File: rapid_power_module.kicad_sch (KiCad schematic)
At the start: 206 parts, among them J1 Conn_02x04_Top_Bottom, J10 JST-GH 4Pin, J11 SWD Header, J12 SWD Header, J16 USB_C_Receptacle_USB2.0, J17 TC2050, J2 Conn_02x03_Odd_Even, J3 Conn_02x04_Top_Bottom, J4 Conn_02x03_Odd_Even, J5 Molex MicroFit 2x2, J6 Molex MicroFit 2x2, J7 Molex MicroFit 2x2, J8 Molex MicroFit 2x2, Q1 AOSP21321, Q12 AOSP21321, Q2 AOSP21321, Q3 AOSP21321, Q4 HiDRV1, Q5 LoDRV1, Q6 HiDRV2, Q7 LoDRV2, SW1 KMR721NGLFS, SW2 KMR721NGLFS, U1 BQ25756RRVR, U10 L7805, U11 MCP2562-E-SN, U12 STM32F105RCTx, U13 AZ1117I-3.3, U14 TPD4E1U06, U15 TPD4E1U06, U2 CYPD3177-24LQ, U3 BQ76952PFBR, Y3 8MHz 12pF

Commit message: more routing work
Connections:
- net CHRG_IND_LED_1: now also U12.54 (PD2); no longer U12.33 (PB12)
- net CHRG_IND_LED_2: now also U12.55 (PB3); no longer U12.34 (PB13)
- net CHRG_IND_LED_3: now also U12.56 (PB4); no longer U12.35 (PB14)
- net CHRG_IND_LED_4: now also U12.57 (PB5); no longer U12.36 (PB15)
- net D0+: now also U14.5 (IO4); no longer U14.4 (IO3)
- net D0-: now also U14.4 (IO3); no longer U14.5 (IO4)
- net INT: now also U12.51 (PC10); no longer U12.25 (PC5)
- net PG: now also U12.36 (PB15); no longer U12.39 (PC8)
- net STAT_LED0: now also U12.33 (PB12); no longer U12.2 (PC13)
- net STAT_LED1: now also U12.34 (PB13); no longer U12.3 (PC14)
- net STAT_LED2: now also U12.35 (PB14); no longer U12.4 (PC15)
- net USB_PD_INTERRUPT: now also U12.29 (PB10); no longer U12.21 (PA5)
- no-connect marks 35 -> 33
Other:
- note added: "Mv usb int from 21 to 29"
- note added: "int from 25 to 51 PG from 39 to 36"

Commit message: more routing
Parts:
- D4: footprint Package_TO_SOT_THT:TO-220-3_Vertical -> Diode_SMD:D_SOD-323; LCSC C5358933 -> C191023
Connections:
- net BREG: now also U12.4 (PC15)
- net REGIN: now also U12.3 (PC14)
- net RST_SHUT: now also U12.2 (PC13); no longer U12.16 (PA2)
- no-connect marks 33 -> 31
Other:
- note added: "int from 25 to 51 PG from 39 to 36 REGIN und BREG verbunden mit STM32"
- note added: "mv 16 -> 2"
- note removed: "int from 25 to 51 PG from 39 to 36"
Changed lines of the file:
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@@
 		)
 	)
-	(text "int from 25 to 51\nPG from 39 to 36"
+	(text "int from 25 to 51\nPG from 39 to 36\nREGIN und BREG verbunden mit STM32"
 		(exclude_from_sim no)
-		(at 113.792 326.644 0)
+		(at 108.458 330.708 0)
 		(effects
 			(font
@@
 		)
 	)
+	(text "mv 16 -> 2"
+		(exclude_from_sim no)
+		(at 171.45 267.97 0)
+		(effects
+			(font
+				(size 1.27 1.27)
+			)
+		)
+	)
 	(text "@todo: take a closer look"
 		(exclude_from_sim no)
@@
 	)
 	(no_connect
-		(at 127 323.85)
-	)
-	(no_connect
 		(at 488.95 130.81)
 	)
@@
 	)
 	(no_connect
+		(at 162.56 270.51)
+	)
+	(no_connect
 		(at 488.95 123.19)
 	)
@@
 	)
 	(no_connect
-		(at 127 318.77)
-	)
-	(no_connect
-		(at 127 321.31)
-	)
-	(no_connect
 		(at 488.95 110.49)
 	)
@@
 	(wire
 		(pts
-			(xy 165.1 270.51) (xy 162.56 270.51)
-		)
-		(stroke
-			(width 0)
-			(type default)
-		)
-	)
-	(wire
-		(pts
 			(xy 205.74 167.64) (xy 203.2 167.64)
 		)
@@
 	(global_label "RST_SHUT"
 		(shape input)
-		(at 165.1 270.51 0)
+		(at 127 318.77 180)
 		(fields_autoplaced yes)
 		(effects
@@
 				(size 1.27 1.27)
 			)
-			(justify left)
+			(justify right)
 		)
 		(property "Intersheetrefs" "${INTERSHEET_REFS}"
-			(at 177.338 270.51 0)
+			(at 114.762 318.77 0)
 			(effects
 				(font
 					(size 1.27 1.27)
 				)
-				(justify left)
+				(justify right)
 				(hide yes)
 			)
@@
 		)
 	)
+	(global_label "REGIN"
+		(shape input)
+		(at 127 321.31 180)
+		(fields_autoplaced yes)
+		(effects
+			(font
+				(size 1.27 1.27)
+			)
+			(justify right)
+		)
+		(property "Intersheetrefs" "${INTERSHEET_REFS}"
+			(at 118.3905 321.31 0)
+			(effects
+				(font
+					(size 1.27 1.27)
+				)
+				(justify right)
+				(hide yes)
+			)
+		)
+	)
 	(global_label "SWCLK"
 		(shape input)
@@
 		)
 	)
+	(global_label "BREG"
+		(shape input)
+		(at 127 323.85 180)
+		(fields_autoplaced yes)
+		(effects
+			(font
+				(size 1.27 1.27)
+			)
+			(justify right)
+		)
+		(property "Intersheetrefs" "${INTERSHEET_REFS}"
+			(at 119.0558 323.85 0)
+			(effects
+				(font
+					(size 1.27 1.27)
+				)
+				(justify right)
+				(hide yes)
+			)
+		)
+	)
 	(global_label "SWDIO"
 		(shape input)
@@
 			)
 		)
-		(property "Footprint" "Package_TO_SOT_THT:TO-220-3_Vertical"
+		(property "Footprint" "Diode_SMD:D_SOD-323"
 			(at 533.4 326.39 0)
 			(effects
@@
 			)
 		)
-		(property "LCSC" "C5358933"
+		(property "LCSC" "C191023"
 			(at 533.4 326.39 0)
 			(effects

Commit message: Fixed Balancer Pins so that LDO is not used and LDO input is grounded
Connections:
- net PGND: now also U3.36 (REGIN), U3.37 (BREG)
- net BREG: no longer names the net of U12.4 (PC15)
- net BREG: no longer U3.37 (BREG)
- net REGIN: no longer names the net of U12.3 (PC14)
- net REGIN: no longer U3.36 (REGIN)
- no-connect marks 31 -> 33
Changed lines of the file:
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@@
 	)
 	(junction
+		(at 490.22 115.57)
+		(diameter 0)
+		(color 0 0 0 0)
+	)
+	(junction
 		(at 233.68 123.19)
 		(diameter 0)
@@
 	)
 	(no_connect
+		(at 127 321.31)
+	)
+	(no_connect
 		(at 488.95 107.95)
 	)
 	(no_connect
+		(at 127 323.85)
+	)
+	(no_connect
 		(at 328.93 368.3)
 	)
@@
 	(wire
 		(pts
+			(xy 490.22 118.11) (xy 490.22 115.57)
+		)
+		(stroke
+			(width 0)
+			(type default)
+		)
+	)
+	(wire
+		(pts
 			(xy 30.48 349.25) (xy 30.48 356.87)
 		)
@@
 	(wire
 		(pts
+			(xy 488.95 118.11) (xy 490.22 118.11)
+		)
+		(stroke
+			(width 0)
+			(type default)
+		)
+	)
+	(wire
+		(pts
 			(xy 62.23 68.58) (xy 62.23 71.12)
 		)
@@
 	(wire
 		(pts
+			(xy 490.22 115.57) (xy 492.76 115.57)
+		)
+		(stroke
+			(width 0)
+			(type default)
+		)
+	)
+	(wire
+		(pts
 			(xy 421.64 378.46) (xy 421.64 379.73)
 		)
@@
 	(wire
 		(pts
+			(xy 490.22 115.57) (xy 488.95 115.57)
+		)
+		(stroke
+			(width 0)
+			(type default)
+		)
+	)
+	(wire
+		(pts
 			(xy 499.11 325.12) (xy 502.92 325.12)
 		)
@@
 	(wire
 		(pts
-			(xy 488.95 115.57) (xy 490.22 115.57)
-		)
-		(stroke
-			(width 0)
-			(type default)
-		)
-	)
-	(wire
-		(pts
 			(xy 353.06 328.93) (xy 353.06 365.76)
 		)
@@
 	(wire
 		(pts
-			(xy 488.95 118.11) (xy 490.22 118.11)
-		)
-		(stroke
-			(width 0)
-			(type default)
-		)
-	)
-	(wire
-		(pts
 			(xy 426.72 379.73) (xy 426.72 381)
 		)
@@
 		)
 	)
-	(global_label "REGIN"
-		(shape input)
-		(at 490.22 118.11 0)
-		(fields_autoplaced yes)
-		(effects
-			(font
-				(size 1.27 1.27)
-			)
-			(justify left)
-		)
-		(property "Intersheetrefs" "${INTERSHEET_REFS}"
-			(at 498.8295 118.11 0)
-			(effects
-				(font
-					(size 1.27 1.27)
-				)
-				(justify left)
-				(hide yes)
-			)
-		)
-	)
 	(global_label "USB_D-"
 		(shape input)
@@
 		)
 	)
-	(global_label "REGIN"
-		(shape input)
-		(at 127 321.31 180)
-		(fields_autoplaced yes)
-		(effects
-			(font
-				(size 1.27 1.27)
-			)
-			(justify right)
-		)
-		(property "Intersheetrefs" "${INTERSHEET_REFS}"
-			(at 118.3905 321.31 0)
-			(effects
-				(font
-					(size 1.27 1.27)
-				)
-				(justify right)
-				(hide yes)
-			)
-		)
-	)
 	(global_label "SWCLK"
 		(shape input)
@@
 		)
 	)
-	(global_label "BREG"
-		(shape input)
-		(at 490.22 115.57 0)
-		(fields_autoplaced yes)
-		(effects
-			(font
-				(size 1.27 1.27)
-			)
-			(justify left)
-		)
-		(property "Intersheetrefs" "${INTERSHEET_REFS}"
-			(at 498.1642 115.57 0)
-			(effects
-				(font
-					(size 1.27 1.27)
-				)
-				(justify left)
-				(hide yes)
-			)
-		)
-	)
 	(global_label "CE"
 		(shape input)
@@
 		)
 	)
-	(global_label "BREG"
-		(shape input)
-		(at 127 323.85 180)
-		(fields_autoplaced yes)
-		(effects
-			(font
-				(size 1.27 1.27)
-			)
-			(justify right)
-		)
-		(property "Intersheetrefs" "${INTERSHEET_REFS}"
-			(at 119.0558 323.85 0)
-			(effects
-				(font
-					(size 1.27 1.27)
-				)
-				(justify right)
-				(hide yes)
-			)
-		)
-	)
 	(global_label "SWDIO"
 		(shape input)
@@
 	)
 	(symbol
+		(lib_id "power:VSS")
+		(at 422.91 132.08 180)
+		(unit 1)
+		(exclude_from_sim no)
+		(in_bom yes)
+		(on_board yes)
+		(dnp no)
+		(property "Reference" "#PWR053"
+			(at 422.91 128.27 0)
+			(effects
+				(font
+					(size 1.27 1.27)
+				)
+				(hide yes)
+			)
+		)
+		(property "Value" "VSS"
+			(at 423.164 135.89 0)
+			(effects
+				(font
+					(size 1.27 1.27)
+				)
+			)
+		)
+		(property "Footprint" ""
+			(at 422.91 132.08 0)
+			(effects
+				(font
+					(size 1.27 1.27)
+				)
+				(hide yes)
+			)
+		)
+		(property "Datasheet" ""
+			(at 422.91 132.08 0)
+			(effects
+				(font
+					(size 1.27 1.27)
+				)
+				(hide yes)
+			)
+		)
+		(property "Description" "Power symbol creates a global label with name \"VSS\""
+			(at 422.91 132.08 0)
+			(effects
+				(font
+					(size 1.27 1.27)
+				)
+				(hide yes)
+			)
+		)
+		(pin "1"
+		)
+		(instances
+			(project "rapid_power_module"
+				(path "/afc8cbd3-9ea8-40a2-afae-ed6bd0fe7e6e"
+					(reference "#PWR053")
+					(unit 1)
+				)
+			)
+		)
+	)
+	(symbol
 		(lib_id "Device:C")
 		(at 158.75 250.19 0)
@@
 	)
 	(symbol
+		(lib_id "power:VSS")
+		(at 492.76 115.57 180)
+		(unit 1)
+		(exclude_from_sim no)
+		(in_bom yes)
+		(on_board yes)
+		(dnp no)
+		(property "Reference" "#PWR052"
+			(at 492.76 111.76 0)
+			(effects
+				(font
+					(size 1.27 1.27)
+				)
+				(hide yes)
+			)
+		)
+		(property "Value" "VSS"
+			(at 493.014 119.38 0)
+			(effects
+				(font
+					(size 1.27 1.27)
+				)
+			)
+		)
+		(property "Footprint" ""
+			(at 492.76 115.57 0)
+			(effects
+				(font
+					(size 1.27 1.27)
+				)
+				(hide yes)
+			)
+		)
+		(property "Datasheet" ""
+			(at 492.76 115.57 0)
+			(effects
+				(font
+					(size 1.27 1.27)
+				)
+				(hide yes)
+			)
+		)
+		(property "Description" "Power symbol creates a global label with name \"VSS\""
+			(at 492.76 115.57 0)
+			(effects
+				(font
+					(size 1.27 1.27)
+				)
+				(hide yes)
+			)
+		)
+		(pin "1"
+		)
+		(instances
+			(project "rapid_power_module"
+				(path "/afc8cbd3-9ea8-40a2-afae-ed6bd0fe7e6e"
+					(reference "#PWR052")
+					(unit 1)
+				)
+			)
+		)
+	)
+	(symbol
 		(lib_id "power:GND")
 		(at 349.25 336.55 0)
@@
 					(unit 1)
 				)
-			)
-		)
-	)
-	(symbol
-		(lib_id "power:GND1")
-		(at 422.91 132.08 0)
-		(mirror y)
-		(unit 1)
-		(exclude_from_sim no)
-		(in_bom yes)
-		(on_board yes)
-		(dnp no)
-		(property "Reference" "#PWR029"
-			(at 422.91 138.43 0)
-			(effects
-				(font
-					(size 1.27 1.27)
-				)
-				(hide yes)
-			)
-		)
-		(property "Value" "PGND"
-			(at 422.91 137.16 0)
-			(effects
-				(font
-					(size 1.27 1.27)
-				)
-			)
-		)
-		(property "Footprint" ""
-			(at 422.91 132.08 0)
-			(effects
-				(font
-					(size 1.27 1.27)
-				)
-				(hide yes)
-			)
-		)
-		(property "Datasheet" ""
-			(at 422.91 132.08 0)
-			(effects
-				(font
-					(size 1.27 1.27)
-				)
-				(hide yes)
-			)
-		)
-		(property "Description" "Power symbol creates a global label with name \"GND1\" , ground"
-			(at 422.91 132.08 0)
-			(effects
-				(font
-					(size 1.27 1.27)
-				)
-				(hide yes)
-			)
-		)
-		(pin "1"
-		)
-		(instances
-			(project "rapid_power_module"
-				(path "/afc8cbd3-9ea8-40a2-afae-ed6bd0fe7e6e"
-					(reference "#PWR029")
-					(unit 1)
-				)

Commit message: Annotated change
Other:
- note added: "Page 75, Pin 36 and 37 <-> VSS"
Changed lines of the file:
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@@
+		)
+	)
+	(text "Page 75, Pin 36 and 37 <-> VSS"
+		(exclude_from_sim no)
+		(at 512.064 115.062 0)
+		(effects
+			(font
+				(size 1.27 1.27)
+			)
 		)
 	)

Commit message: more routing
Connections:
- net +3.3V: no longer J17.7 (Pin_7), J17.8 (Pin_8), R14.1, R15.1, R16.1, R17.1, R26.1, R39.1, R40.1, R42.1, R64.1, R69.1, R70.1, R72.1, R89.1, R90.1
- net +3V3: now also J17.7 (Pin_7), J17.8 (Pin_8), R14.1, R15.1, R16.1, R17.1, R26.1, R39.1, R40.1, R42.1, R64.1, R69.1, R70.1, R72.1, R89.1, R90.1
- net GND: now also C11.2, C12.2, C13.2, C19.1, C20.2, C21.1, C24.1, C58.1, C59.1, C60.2, C61.1, C67.2, C68.2, C69.2, C70.2, C71.2, C72.2, C73.2, C74.2, C75.2, C76.2, C77.2, C78.2, C79.1, C80.1, D20.1 (K), D21.1 (K), D24.2 (A), H1.1, H2.1, H3.1, H4.1, J1.1 (Pin_1), J1.2 (Pin_2), J11.4 (Pin_4), J12.4 (Pin_4), J16.A1 (GND), J16.A12 (GND), J16.B1 (GND), J16.B12 (GND), J16.S1 (SHIELD), J17.3 (Pin_3), J17.4 (Pin_4), J3.1 (Pin_1), J3.2 (Pin_2), R13.2, R19.2, R23.2, R24.2, R25.2, R27.2, R31.2, R43.2, R7.2, R76.1, R83.2, R91.1, R94.2, R95.2, R96.2, R97.2, R98.2, SW2.1 (A), U1.22 (PGND), U10.2 (GND), U11.2 (VSS), U11.8 (STBY), U12.12 (VSSA), U12.18 (VSS), U12.31 (VSS), U12.47 (VSS), U12.63 (VSS), U13.1 (GND), U14.3 (GND), U15.3 (GND), U2.19 (GND), U2.22 (GND), U2.25 (GND), U2.6 (ISNK_FINE), U3.17 (VSS), U3.18 (SRP), U3.20 (SRN), U3.36 (REGIN), U3.37 (BREG), U3.41 (LD), Y3.2, Y3.4
- net J1-SWDIO: now also U15.1 (IO1); no longer U15.2 (IO2)
- net J1-SWO: now also U15.2 (IO2); no longer U15.1 (IO1)
- net PGND: no longer C11.2, C12.2, C13.2, C19.1, C20.2, C21.1, C24.1, C58.1, C59.1, C60.2, C61.1, C67.2, C68.2, C69.2, C70.2, C71.2, C72.2, C73.2, C74.2, C75.2, C76.2, C77.2, C78.2, C79.1, C80.1, D20.1 (K), D21.1 (K), D24.2 (A), H1.1, H2.1, H3.1, H4.1, J1.1 (Pin_1), J1.2 (Pin_2), J11.4 (Pin_4), J12.4 (Pin_4), J16.A1 (GND), J16.A12 (GND), J16.B1 (GND), J16.B12 (GND), J16.S1 (SHIELD), J17.3 (Pin_3), J17.4 (Pin_4), J3.1 (Pin_1), J3.2 (Pin_2), R13.2, R19.2, R23.2, R24.2, R25.2, R27.2, R31.2, R43.2, R7.2, R76.1, R83.2, R91.1, R94.2, R95.2, R96.2, R97.2, R98.2, SW2.1 (A), U1.22 (PGND), U10.2 (GND), U11.2 (VSS), U11.8 (STBY), U12.12 (VSSA), U12.18 (VSS), U12.31 (VSS), U12.47 (VSS), U12.63 (VSS), U13.1 (GND), U14.3 (GND), U15.3 (GND), U2.19 (GND), U2.22 (GND), U2.25 (GND), U2.6 (ISNK_FINE), U3.17 (VSS), U3.18 (SRP), U3.20 (SRN), U3.36 (REGIN), U3.37 (BREG), U3.41 (LD), Y3.2, Y3.4
- net STAT1: now also U12.38 (PC7); no longer U12.37 (PC6)
- net STAT2: now also U12.37 (PC6); no longer U12.38 (PC7)
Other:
- note added: "@TODO sinnvoll?"

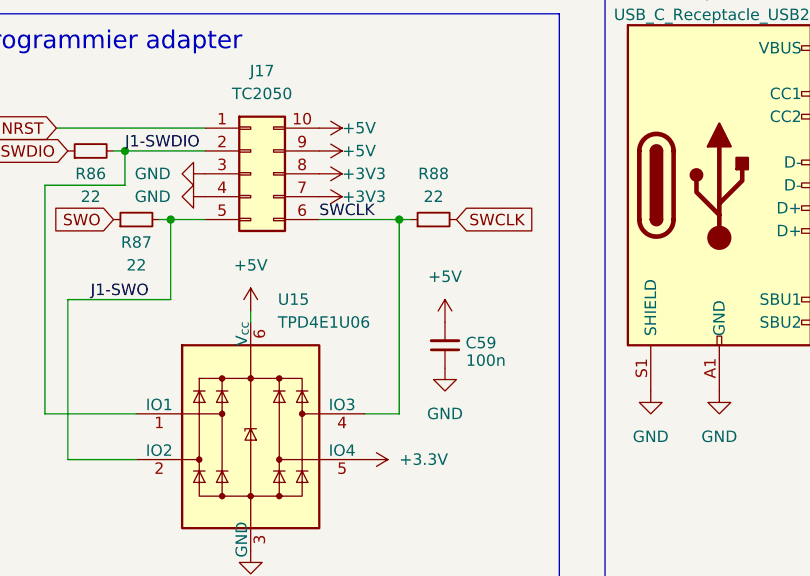
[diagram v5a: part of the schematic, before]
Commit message: improve area shapes
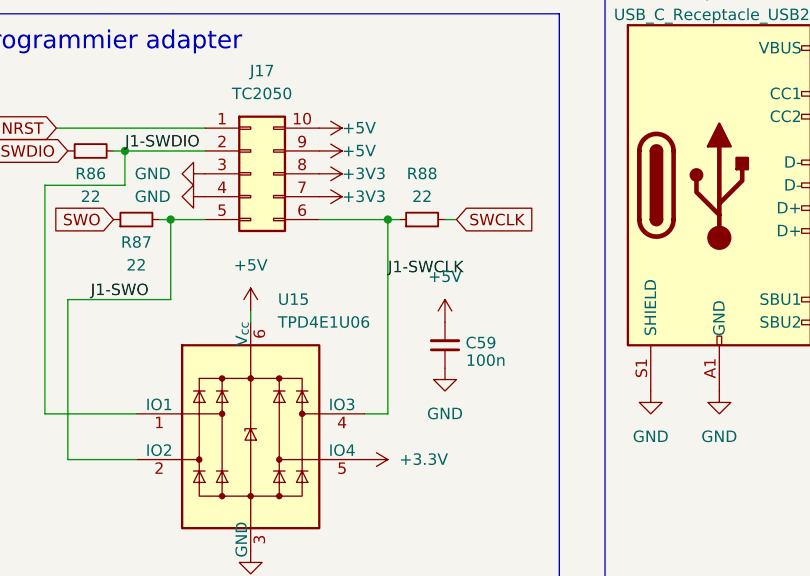
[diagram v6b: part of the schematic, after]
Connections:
- net SWCLK: no longer J17.6 (Pin_6), R88.1, U15.4 (IO3)
- new net J1-SWCLK: J17.6 (Pin_6), R88.1, U15.4 (IO3)
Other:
- moved on the sheet: R88
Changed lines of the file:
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@@
 	)
 	(junction
+		(at 276.86 356.87)
+		(diameter 0)
+		(color 0 0 0 0)
+	)
+	(junction
 		(at 62.23 59.69)
 		(diameter 0)
@@
 	)
 	(junction
-		(at 278.13 356.87)
-		(diameter 0)
-		(color 0 0 0 0)
-	)
-	(junction
 		(at 170.18 245.11)
 		(diameter 0)
@@
 	(wire
 		(pts
-			(xy 278.13 378.46) (xy 274.32 378.46)
+			(xy 276.86 378.46) (xy 274.32 378.46)
 		)
 		(stroke
@@
 	(wire
 		(pts
+			(xy 283.21 356.87) (xy 284.48 356.87)
+		)
+		(stroke
+			(width 0)
+			(type default)
+		)
+	)
+	(wire
+		(pts
 			(xy 278.13 207.01) (xy 278.13 209.55)
 		)
@@
 	(wire
 		(pts
+			(xy 276.86 356.87) (xy 278.13 356.87)
+		)
+		(stroke
+			(width 0)
+			(type default)
+		)
+	)
+	(wire
+		(pts
 			(xy 529.59 304.8) (xy 529.59 306.07)
 		)
@@
 	(wire
 		(pts
-			(xy 278.13 356.87) (xy 279.4 356.87)
-		)
-		(stroke
-			(width 0)
-			(type default)
-		)
-	)
-	(wire
-		(pts
 			(xy 162.56 308.61) (xy 193.04 308.61)
 		)
@@
 	(wire
 		(pts
-			(xy 269.24 356.87) (xy 278.13 356.87)
+			(xy 269.24 356.87) (xy 276.86 356.87)
 		)
 		(stroke
@@
 	(wire
 		(pts
-			(xy 278.13 356.87) (xy 278.13 378.46)
+			(xy 276.86 356.87) (xy 276.86 378.46)
 		)
 		(stroke
@@
 		)
 	)
-	(label "SWCLK"
-		(at 269.24 356.87 0)
+	(label "J1-SWCLK"
+		(at 276.86 363.22 0)
 		(effects
 			(font
@@
 	(symbol
 		(lib_id "Device:R_Small")
-		(at 281.94 356.87 90)
+		(at 280.67 356.87 90)
 		(unit 1)
 		(exclude_from_sim no)
@@
 		(fields_autoplaced yes)
 		(property "Reference" "R88"
-			(at 281.94 351.79 90)
+			(at 280.67 351.79 90)
 			(effects
 				(font
@@
 		)
 		(property "Value" "22"
-			(at 281.94 354.33 90)
+			(at 280.67 354.33 90)
 			(effects
 				(font
@@
 		)
 		(property "Footprint" "Resistor_SMD:R_0402_1005Metric"
-			(at 281.94 356.87 0)
+			(at 280.67 356.87 0)
 			(effects
 				(font
@@
 		)
 		(property "Datasheet" "~"
-			(at 281.94 356.87 0)
+			(at 280.67 356.87 0)
 			(effects
 				(font
@@
 		)
 		(property "Description" ""
-			(at 281.94 356.87 0)
+			(at 280.67 356.87 0)
 			(effects
 				(font
@@
 		)
 		(property "Manufacturer" "YAGEO"
-			(at 281.94 356.87 0)
+			(at 280.67 356.87 0)
 			(effects
 				(font
@@
 		)
 		(property "Part#" "RC0603FR-0710KL"
-			(at 281.94 356.87 0)
+			(at 280.67 356.87 0)
 			(effects
 				(font
@@
 		)
 		(property "LCSC" "C25092"
-			(at 281.94 356.87 0)
+			(at 280.67 356.87 0)
 			(effects
 				(font

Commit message: gnd changes in scematic and routing, tbc
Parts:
- added NT1: NetTie_2, NetTie:NetTie-2_SMD_Pad0.5mm, symbol Device:NetTie_2
- added R77, R78: 22R, Resistor_SMD:R_0402_1005Metric, symbol Device:R_Small
- added U16: TPD4E1U06, Package_TO_SOT_SMD:SOT-563, symbol stigma:TPD4E001DRL
- R22: value 10 -> 10R
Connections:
- net +5V: now also U16.6 (V_{cc})
- net +VSW: no longer FB3.2
- net CAN+: now also U16.4 (IO3)
- net CAN-: now also U16.5 (IO4)
- net GND: now also C16.2, C17.1, C81.2, C82.2, C83.2, U16.3 (GND); no longer R25.2, R27.2, R31.2, R43.2, R83.2, R94.2, R95.2, R96.2, R97.2, R98.2, U1.22 (PGND)
- net I2C_SCL: now also R78.1, U16.1 (IO1); no longer J12.2 (Pin_2)
- net I2C_SDA: now also R77.1, U16.2 (IO2); no longer J12.3 (Pin_3)
- net PACK+: now also FB3.2
- net PGND: now also R25.2, R27.2, R31.2, R43.2, R83.2, R94.2, R95.2, R96.2, R97.2, R98.2, U1.22 (PGND); no longer BT3.N (-), C16.2, C17.1, C81.2, C82.2, C83.2, C84.2, C85.2, C86.2, C87.2, C88.2, C89.2, C90.2, C91.2, J10.3 (Pin_3), J10.4 (Pin_4), J6.1 (Pin_1), J6.2 (Pin_2), J8.1 (Pin_1), J8.2 (Pin_2), R20.1
- net USB_PD_INTERRUPT: now also U12.21 (PA5); no longer U12.29 (PB10)
- new net: J12.3 (Pin_3), R77.2
- new net: J12.2 (Pin_2), R78.2
- new net SYS_GND: BT3.N (-), C84.2, C85.2, C86.2, C87.2, C88.2, C89.2, C90.2, C91.2, J10.3 (Pin_3), J10.4 (Pin_4), J6.1 (Pin_1), J6.2 (Pin_2), J8.1 (Pin_1), J8.2 (Pin_2), R20.1
- no-connect marks 33 -> 34
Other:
- note added: ""If not used, these pins should be connected to pin 17 (VSS)""
- note added: "@TODO: ?!"
- note added: "@TODO: Formel auf Seite 64 checken und Widerstände anpassen"
- note added: "RAPID Power Board"
- note added: "TODO: Sicherung"
- note added: "USB PD:"
- note added: "arming connector"
- note added: "connectors"
- note added: "controller"
- note added: "input diodes"
- note added: "mounting"
- note added: "power connectors"
- note added: "programming adapters"
- note added: "test points"
- note removed: "@TODO können C4 und C7 nicht den selben Footprint nutzen?"
- note removed: "@TODO sinnvoll?"
- note removed: "@todo add proper supply, decide if using regn is sufficient"
- note removed: "@todo probabyl add few condensators"
- note removed: "Connectors"
- note removed: "Controller"
- note removed: "Formel auf Seite 64 checken und Widerstände anpassen"
- note removed: "Input Diodes"
- note removed: "Mv usb int from 21 to 29"
- note removed: "Programmier adapter"
- note removed: "TODO: SIcherung"
- note removed: "TODO: figure out on which voltage outputs diodes are needed"
- note removed: "USB PD"
- note removed: "reverse current: 0.3 mA TODO: Is that low enough?"
- moved on the sheet: BT1, BT2, BT3, C1, C10, C11, C12, C13, C14, C15, C16, C17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

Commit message: some changes in the scematic
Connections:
- net +3.3V is gone; now on net +3V3: U15.5 (IO4)
- net GND: no longer R91.1
- net PGND: now also R91.1
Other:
- note added: "Ensure, that no current can flow inbetween inputs"
- note added: "Regulators"
- note removed: ""If not used, these pins should be connected to pin 17 (VSS)""
- note removed: "Ensure, that no current can flow from one input to the other"
- note removed: "Regulator"
- moved on the sheet: BT1, BT2, BT3, C1, C14, C15, C16, C17, C18, C19, C2, C21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
